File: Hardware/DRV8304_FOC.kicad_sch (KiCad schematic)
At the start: 64 parts, among them J1 Conn_01x02, J2 Conn_01x03, J3 Conn_01x03, J4 Conn_02x07_Counter_Clockwise, Q1 SIRA18ADP, Q2 SIRA18ADP, Q3 SIRA18ADP, Q4 SIRA18ADP, Q5 SIRA18ADP, Q6 SIRA18ADP, SW2 SW_Push, U1 TPS565208, U2 TPS259850RQPR, U3 DRV8304HRHAR, U4 STM32F412CEUx, U5 AS5055A, Y1 Crystal_GND23

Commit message: Added Board outline DXF and test points
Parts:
- removed J2: Conn_01x03, Connector_JST:JST_XH_S3B-XH-A-1_1x03_P2.50mm_Horizontal, symbol Connector_Generic:Conn_01x03
- added C23, C24: 0.1uF, Capacitor_SMD:C_0402_1005Metric, symbol Device:C
- added TP1, TP2, TP3, TP4, TP5, TP6, TP7, TP8, TP9: TestPoint, TestPoint:TestPoint_Pad_D1.0mm, symbol Connector:TestPoint
- Q1, Q2, Q3, Q4, Q5, Q6: symbol Simulation_SPICE:NMOS -> 1_MyLib:NMOS_PPAK_SO8
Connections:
- net MOSI is gone; now on net SPI_MOSI: R9.1
- net SCK is gone; now on net SPI_SCK: R10.1
- net ~{SS} is gone; now on net SPI_~{SS}: U5.4 (~{SS})
- net GHA: now also Q1.4 (G)
- net GLA: now also Q2.4 (G)
- net GND: now also J3.1 (Pin_1), C23.1, C24.1
- net Vin: now also Q1.5 (D), Q3.5 (D), Q5.5 (D); no longer Q1.1 (D), Q3.1 (D), Q5.1 (D)
- net at R22.1: now also U4.40 (PB4); no longer U5.2 (MISO)
- net ISENSE_C: now reaches U3.21 (SOC)
- net ISENSE_C: now also U4.13 (PA3), TP7.1
- net ISENSE_B: now reaches U3.22 (SOB)
- net ISENSE_B: now also U4.14 (PA4), TP8.1
- net ISENSE_A: now reaches U3.23 (SOA)
- net ISENSE_A: now also U4.15 (PA5), TP9.1
- net INHA: now reaches U3.34 (INHA)
- net INHA: now also U4.29 (PA8), TP1.1
- net INLA: now reaches U3.35 (INLA)
- net INLA: now also U4.26 (PB13), TP2.1
- net INHB: now reaches U3.36 (INHB)
- net INHB: now also U4.30 (PA9), TP3.1
- net INLB: now reaches U3.37 (INLB)
- net INLB: now also U4.27 (PB14), TP4.1
- net INHC: now reaches U3.38 (INHC)
- net INHC: now also U4.31 (PA10), TP5.1
- net INLC: now reaches U3.39 (INLC)
- net INLC: now also U4.28 (PB15), TP6.1
- net at Q2.3 (S), R11.1: now also Q2.1 (S), Q2.2 (S)
- net at Q1.2 (S): now also Q1.1 (S), Q1.3 (S), Q2.5 (D)
- net at Q6.1 (S): now also Q6.2 (S), Q6.3 (S), R13.1; no longer Q5.3 (S)
- net at Q4.1 (S): now also Q4.2 (S), Q4.3 (S), R12.1; no longer Q3.3 (S)
- net at Y1.1: now also U4.5 (PH0), C24.2
- net at Y1.4: now also U4.6 (PH1), C23.2
- net at Q3.2 (S): now also Q3.1 (S), Q3.3 (S), Q4.5 (D)
- net UART_RX: now reaches J3.2 (Pin_2)
- net UART_RX: now also U4.43 (PB7)
- net UART_TX: now reaches J3.3 (Pin_3)
- net UART_TX: now also U4.45 (PB8)
- net SPI_~{SS}: now reaches U4.20 (PB2)
- net SPI_SCK: now reaches U4.39 (PB3)
- net SPI_MOSI: now reaches U4.41 (PB5)
- net at Q5.2 (S): now also Q5.1 (S), Q5.3 (S), Q6.5 (D)
- net MISO renamed SPI_MISO
- net SPI_MISO: now also U5.2 (MISO)
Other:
- moved on the sheet: J3, J4, R15, U3, Y1

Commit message: Routing update
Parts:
- TP1, TP2, TP3, TP4, TP5, TP6, TP7, TP8, TP9: footprint TestPoint:TestPoint_Pad_D1.0mm -> MyLib:TestPoint_1mm
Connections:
- net GHB: now also Q3.4 (G)
- net GHC: now also Q5.4 (G)
- net GLB: now also Q4.4 (G)
- net GLC: now also Q6.4 (G)
- net INHA: now also U4.31 (PA10); no longer U4.29 (PA8)
- net INHC: now also U4.29 (PA8); no longer U4.31 (PA10)
- net INLA: now also U4.28 (PB15); no longer U4.26 (PB13)
- net INLC: now also U4.26 (PB13); no longer U4.28 (PB15)
- net SHA: now also Q1.1 (S), Q1.2 (S), Q1.3 (S), Q2.5 (D)
- net SHB: now also Q3.1 (S), Q3.2 (S), Q3.3 (S), Q4.5 (D)
- net SHC: now also Q5.1 (S), Q5.2 (S), Q5.3 (S), Q6.5 (D)

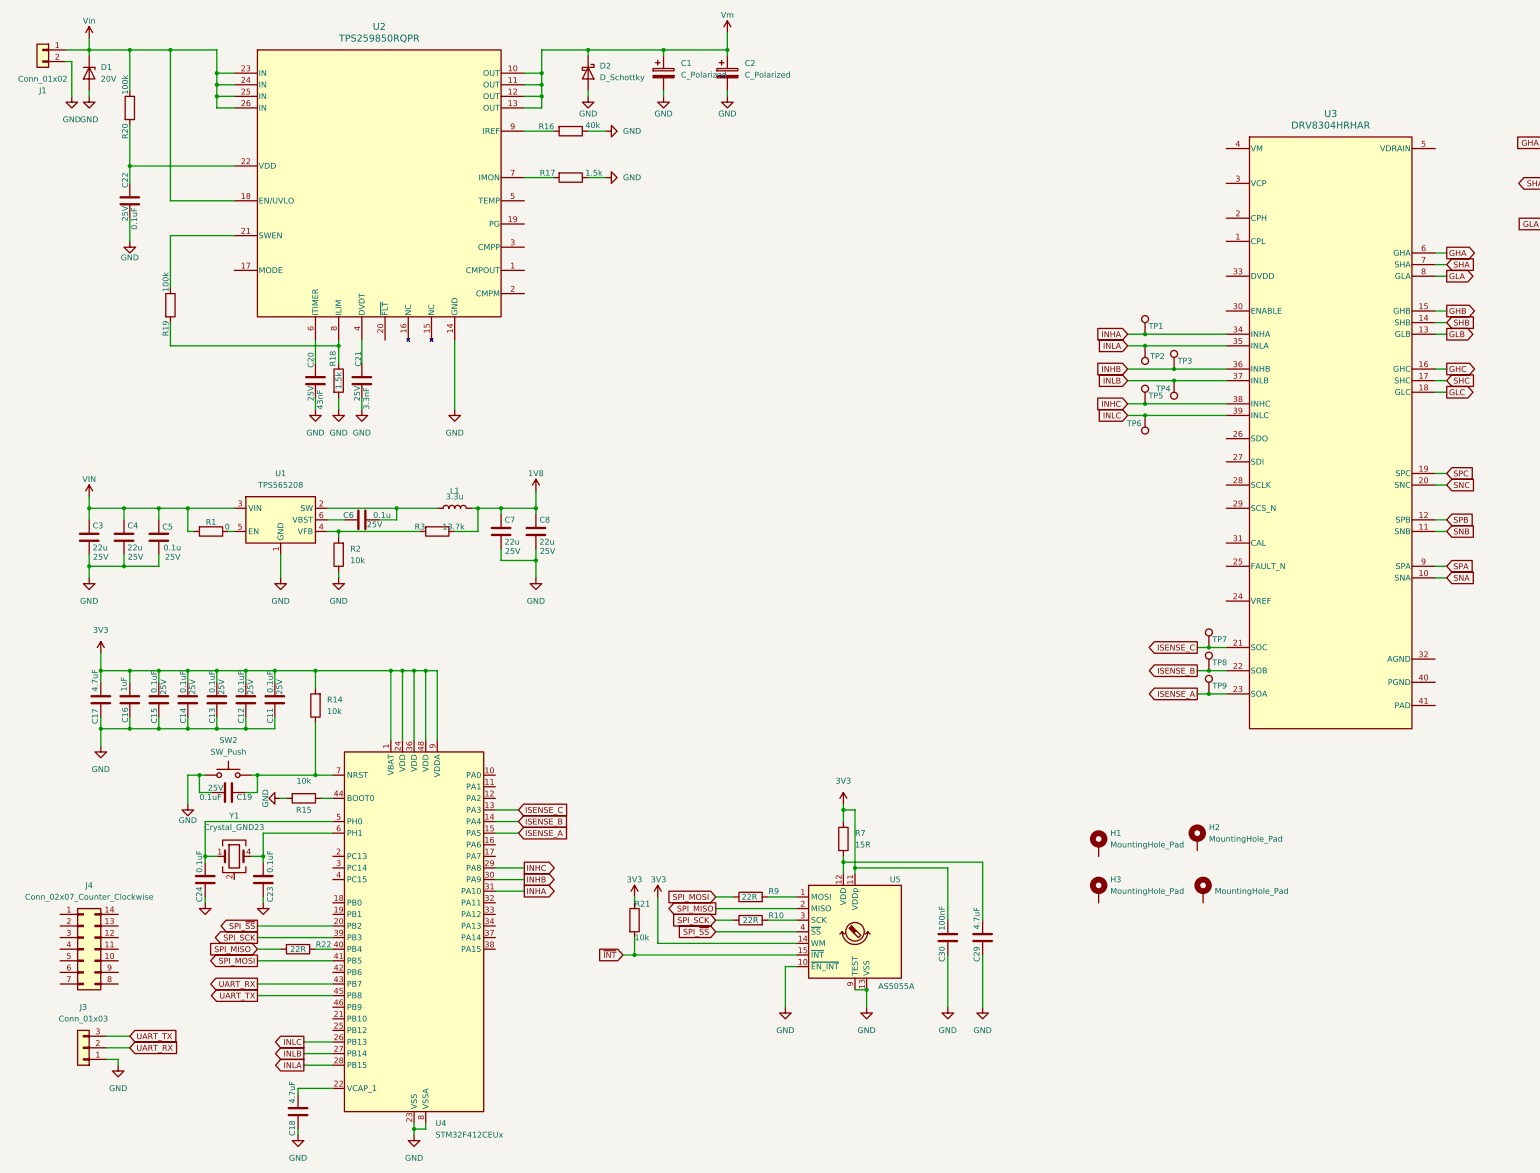
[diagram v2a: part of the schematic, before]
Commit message: Remove EFUSE
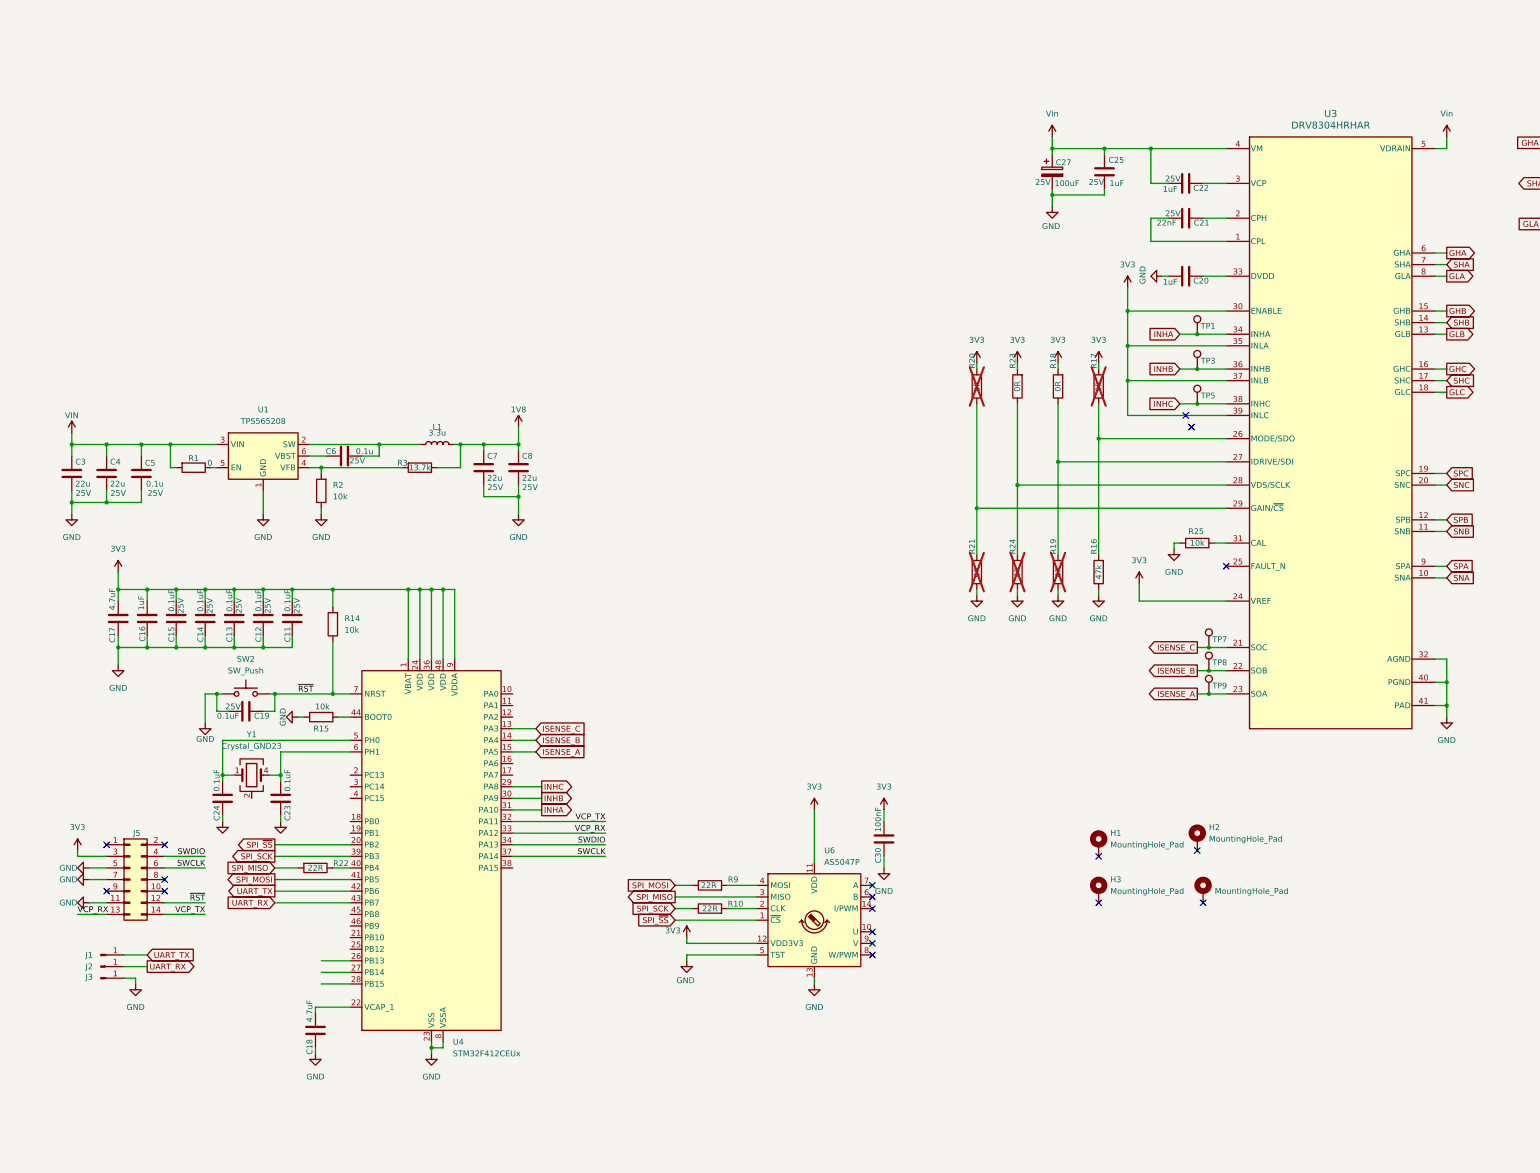
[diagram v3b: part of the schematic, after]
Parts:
- removed C1, C2: C_Polarized, Capacitor_SMD:CP_Elec_6.3x7.7, symbol Device:C_Polarized
- removed C29: 4.7uF, Capacitor_SMD:C_0603_1608Metric, symbol Device:C
- removed D1: 20V, Diode_SMD:D_SMA, symbol Device:D_Zener
- removed D2: D_Schottky, Diode_SMD:D_SMA, symbol Device:D_Schottky
- removed J1: Conn_01x02, Connector_AMASS:AMASS_XT30U-M_1x02_P5.0mm_Vertical, symbol Connector_Generic:Conn_01x02
- removed J3: Conn_01x03, Connector_JST:JST_PH_S3B-PH-K_1x03_P2.00mm_Horizontal, symbol Connector_Generic:Conn_01x03
- removed J4: Conn_02x07_Counter_Clockwise, Connector_PinHeader_1.27mm:PinHeader_2x07_P1.27mm_Vertical_SMD, symbol Connector_Generic:Conn_02x07_Counter_Clockwise
- removed R7: 15R, Resistor_SMD:R_0402_1005Metric, symbol Device:R
- removed TP2, TP4, TP6: TestPoint, MyLib:TestPoint_1mm, symbol Connector:TestPoint
- removed U2: TPS259850RQPR, 1_MyLib:RQP0026A-MFG, symbol 1_MyLib:TPS259850RQPR
- removed U5: AS5055A, Package_DFN_QFN:QFN-16-1EP_4x4mm_P0.65mm_EP2.7x2.7mm, symbol Sensor_Magnetic:AS5055A
- added C25: 1uF, Capacitor_SMD:C_0603_1608Metric, symbol Device:C
- added C27: 100uF, Capacitor_SMD:CP_Elec_6.3x7.7, symbol Device:C_Polarized
- added J1, J2, J3: Conn_01x01_Pin, Connector_Wire:SolderWirePad_1x01_SMD_1x2mm, symbol Connector:Conn_01x01_Pin
- added J5: Conn_02x07_Odd_Even, Connector_PinHeader_1.27mm:PinHeader_2x07_P1.27mm_Vertical_SMD, symbol Connector_Generic:Conn_02x07_Odd_Even
- added R23, R24: 0R, Resistor_SMD:R_0402_1005Metric, symbol Device:R
- added R25: 10k, Resistor_SMD:R_0402_1005Metric, symbol Device:R
- added U6: AS5047P, Package_SO:TSSOP-14_4.4x5mm_P0.65mm, symbol Sensor_Magnetic:AS5047D
- C20: value 43nF -> 1uF; footprint Capacitor_SMD:C_0402_1005Metric -> Capacitor_SMD:C_0603_1608Metric; Voltage Rating 25V -> (none)
- C21: value 3.3nF -> 22nF
- C22: value 0.1uF -> 1uF; footprint Capacitor_SMD:C_0402_1005Metric -> Capacitor_SMD:C_0603_1608Metric
- R16: value 40k -> 47k
- R17: value 1.5k -> 0R; now not fitted
- R18: value 1.5k -> 0R
- R19, R20: value 100k -> 0R; now not fitted
- R21: value 10k -> 0R; now not fitted
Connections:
- net ~{INT} is gone; now on an unnamed net: R21.2
- net 3V3: now also R17.2, R18.2, R20.2, U3.24 (VREF), U3.30 (ENABLE), U3.35 (INLA), U3.37 (INLB), U3.39 (INLC), J5.3 (Pin_3), R23.2, U6.11 (VDD), U6.12 (VDD3V3); no longer R21.1
- net GND: now also C20.1, R19.1, R21.1, U3.32 (AGND), U3.40 (PGND), U3.41 (PAD), C25.1, C27.2, J3.1 (Pin_1), J5.11 (Pin_11), J5.5 (Pin_5), J5.7 (Pin_7), R24.1, R25.2, U6.13 (GND), U6.5 (TST); no longer C20.2, C21.2, C22.2, R17.1, R18.2
- net SPI_MISO: now also U6.3 (MISO)
- net SPI_~{SS}: now also U6.1 (~{CS})
- net UART_RX: now also J2.1 (Pin_1)
- net UART_TX: now also U4.42 (PB6), J1.1 (Pin_1); no longer U4.45 (PB8)
- net Vin: now also C22.1, U3.4 (VM), U3.5 (VDRAIN), C25.2, C27.1; no longer R20.1
- net ~{RST}: now reaches C19.1, R14.1, SW2.2, U4.7 (NRST)
- net ~{RST}: now also J5.12 (Pin_12)
- net at R18.1, R19.2: now also U3.27 (IDRIVE/SDI)
- net at R16.2: now also R17.1, U3.26 (MODE/SDO)
- net at U3.1 (CPL): now also C21.2
- net at U3.2 (CPH): now also C21.1
- net at U3.28 (VDS/SCLK): now also R23.1, R24.2
- net at U3.29 (GAIN/~{CS}): now also R20.1
- net at U3.3 (VCP): now also C22.2
- net at U3.31 (CAL): now also R25.1
- net at U3.33 (DVDD): now also C20.2
- net at R9.2: now also U6.4 (MOSI)
- net at R10.2: now also U6.2 (CLK)
- net VCP_TX: now reaches U4.32 (PA11)
- net VCP_TX: now also J5.14 (Pin_14)
- net VCP_RX: now reaches U4.33 (PA12)
- net VCP_RX: now also J5.13 (Pin_13)
- net SWDIO: now reaches U4.34 (PA13)
- net SWDIO: now also J5.4 (Pin_4)
- net SWCLK: now reaches U4.37 (PA14)
- net SWCLK: now also J5.6 (Pin_6)
- net INLA: no longer names the net of U4.28 (PB15)
- net INLA: no longer U3.35 (INLA)
- net INLB: no longer names the net of U4.27 (PB14)
- net INLB: no longer U3.37 (INLB)
- net INLC: no longer names the net of U4.26 (PB13)
- net INLC: no longer U3.39 (INLC)
- no-connect marks 0 -> 18
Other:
- moved on the sheet: C11, C12, C13, C14, C15, C16, C17, C18, C19, C23, C24, C3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
